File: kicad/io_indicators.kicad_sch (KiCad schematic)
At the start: 68 parts

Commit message: Pick JLCPCB parts for the whole BOM and add BOM/CPL generation
Adds bom/parts.csv (LCSC numbers and MPNs), scripts to apply it to the schematic and
board and to generate the JLCPCB BOM, CPL and a live stock report. Swaps the
BOOTSEL/RESET switch to a basic 5.1 mm part with a matching footprint, and replaces
out-of-stock parts (SS54, WS2812B, 10u caps, SWD header).

Co-Authored-By: Claude Sonnet 5.5 <noreply@anthropic.com>
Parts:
- R100, R101, R72, R73, R74, R75, R76, R77, R78, R79, R80, R81, R82, R83, R84, R85, R86, R87, R88, R89, R90, R91, R92, R93, R94, R95, R96, R97, R98, R99: LCSC (none) -> C25117; MPN (none) -> 0402WGF4700TCE
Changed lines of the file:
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@@
+      (effects (font (size 1.27 1.27)) hide)
+    )
+    (property "LCSC" "C25117" (id 4) (at 40.132 76.2 0)
+      (effects (font (size 1.27 1.27)) hide)
+    )
+    (property "MPN" "0402WGF4700TCE" (id 5) (at 40.132 76.2 0)
       (effects (font (size 1.27 1.27)) hide)
     )
@@
       (effects (font (size 1.27 1.27)) hide)
     )
+    (property "LCSC" "C25117" (id 4) (at 65.532 76.2 0)
+      (effects (font (size 1.27 1.27)) hide)
+    )
+    (property "MPN" "0402WGF4700TCE" (id 5) (at 65.532 76.2 0)
+      (effects (font (size 1.27 1.27)) hide)
+    )
     (pin "1")
     (pin "2")
@@
       (effects (font (size 1.27 1.27)) hide)
     )
+    (property "LCSC" "C25117" (id 4) (at 90.932 76.2 0)
+      (effects (font (size 1.27 1.27)) hide)
+    )
+    (property "MPN" "0402WGF4700TCE" (id 5) (at 90.932 76.2 0)
+      (effects (font (size 1.27 1.27)) hide)
+    )
     (pin "1")
     (pin "2")
@@
       (effects (font (size 1.27 1.27)) hide)
     )
+    (property "LCSC" "C25117" (id 4) (at 116.332 76.2 0)
+      (effects (font (size 1.27 1.27)) hide)
+    )
+    (property "MPN" "0402WGF4700TCE" (id 5) (at 116.332 76.2 0)
+      (effects (font (size 1.27 1.27)) hide)
+    )
     (pin "1")
     (pin "2")
@@
       (effects (font (size 1.27 1.27)) hide)
     )
+    (property "LCSC" "C25117" (id 4) (at 141.732 76.2 0)
+      (effects (font (size 1.27 1.27)) hide)
+    )
+    (property "MPN" "0402WGF4700TCE" (id 5) (at 141.732 76.2 0)
+      (effects (font (size 1.27 1.27)) hide)
+    )
     (pin "1")
     (pin "2")
@@
       (effects (font (size 1.27 1.27)) hide)
     )
+    (property "LCSC" "C25117" (id 4) (at 167.132 76.2 0)
+      (effects (font (size 1.27 1.27)) hide)
+    )
+    (property "MPN" "0402WGF4700TCE" (id 5) (at 167.132 76.2 0)
+      (effects (font (size 1.27 1.27)) hide)
+    )
     (pin "1")
     (pin "2")
@@
       (effects (font (size 1.27 1.27)) hide)
     )
+    (property "LCSC" "C25117" (id 4) (at 192.532 76.2 0)
+      (effects (font (size 1.27 1.27)) hide)
+    )
+    (property "MPN" "0402WGF4700TCE" (id 5) (at 192.532 76.2 0)
+      (effects (font (size 1.27 1.27)) hide)
+    )
     (pin "1")
     (pin "2")
@@
       (effects (font (size 1.27 1.27)) hide)
     )
+    (property "LCSC" "C25117" (id 4) (at 217.932 76.2 0)
+      (effects (font (size 1.27 1.27)) hide)
+    )
+    (property "MPN" "0402WGF4700TCE" (id 5) (at 217.932 76.2 0)
+      (effects (font (size 1.27 1.27)) hide)
+    )
     (pin "1")
     (pin "2")
@@
       (effects (font (size 1.27 1.27)) hide)
     )
+    (property "LCSC" "C25117" (id 4) (at 243.332 76.2 0)
+      (effects (font (size 1.27 1.27)) hide)
+    )
+    (property "MPN" "0402WGF4700TCE" (id 5) (at 243.332 76.2 0)
+      (effects (font (size 1.27 1.27)) hide)
+    )
     (pin "1")
     (pin "2")
@@
       (effects (font (size 1.27 1.27)) hide)
     )
+    (property "LCSC" "C25117" (id 4) (at 268.732 76.2 0)
+      (effects (font (size 1.27 1.27)) hide)
+    )
+    (property "MPN" "0402WGF4700TCE" (id 5) (at 268.732 76.2 0)
+      (effects (font (size 1.27 1.27)) hide)
+    )
     (pin "1")
     (pin "2")
@@
       (effects (font (size 1.27 1.27)) hide)
     )
+    (property "LCSC" "C25117" (id 4) (at 40.132 132.08 0)
+      (effects (font (size 1.27 1.27)) hide)
+    )
+    (property "MPN" "0402WGF4700TCE" (id 5) (at 40.132 132.08 0)
+      (effects (font (size 1.27 1.27)) hide)
+    )
     (pin "1")
     (pin "2")
@@
       (effects (font (size 1.27 1.27)) hide)
     )
+    (property "LCSC" "C25117" (id 4) (at 65.532 132.08 0)
+      (effects (font (size 1.27 1.27)) hide)
+    )
+    (property "MPN" "0402WGF4700TCE" (id 5) (at 65.532 132.08 0)
+      (effects (font (size 1.27 1.27)) hide)
+    )
     (pin "1")
     (pin "2")
@@
       (effects (font (size 1.27 1.27)) hide)
     )
+    (property "LCSC" "C25117" (id 4) (at 90.932 132.08 0)
+      (effects (font (size 1.27 1.27)) hide)
+    )
+    (property "MPN" "0402WGF4700TCE" (id 5) (at 90.932 132.08 0)
+      (effects (font (size 1.27 1.27)) hide)
+    )
     (pin "1")
     (pin "2")
@@
       (effects (font (size 1.27 1.27)) hide)
     )
+    (property "LCSC" "C25117" (id 4) (at 116.332 132.08 0)
+      (effects (font (size 1.27 1.27)) hide)
+    )
+    (property "MPN" "0402WGF4700TCE" (id 5) (at 116.332 132.08 0)
+      (effects (font (size 1.27 1.27)) hide)
+    )
     (pin "1")
     (pin "2")
@@
       (effects (font (size 1.27 1.27)) hide)
     )
+    (property "LCSC" "C25117" (id 4) (at 141.732 132.08 0)
+      (effects (font (size 1.27 1.27)) hide)
+    )
+    (property "MPN" "0402WGF4700TCE" (id 5) (at 141.732 132.08 0)
+      (effects (font (size 1.27 1.27)) hide)
+    )
     (pin "1")
     (pin "2")
@@
       (effects (font (size 1.27 1.27)) hide)
     )
+    (property "LCSC" "C25117" (id 4) (at 167.132 132.08 0)
+      (effects (font (size 1.27 1.27)) hide)
+    )
+    (property "MPN" "0402WGF4700TCE" (id 5) (at 167.132 132.08 0)
+      (effects (font (size 1.27 1.27)) hide)
+    )
     (pin "1")
     (pin "2")
@@
       (effects (font (size 1.27 1.27)) hide)
     )
+    (property "LCSC" "C25117" (id 4) (at 192.532 132.08 0)
+      (effects (font (size 1.27 1.27)) hide)
+    )
+    (property "MPN" "0402WGF4700TCE" (id 5) (at 192.532 132.08 0)
+      (effects (font (size 1.27 1.27)) hide)
+    )
     (pin "1")
     (pin "2")
@@
       (effects (font (size 1.27 1.27)) hide)
     )
+    (property "LCSC" "C25117" (id 4) (at 217.932 132.08 0)
+      (effects (font (size 1.27 1.27)) hide)
+    )
+    (property "MPN" "0402WGF4700TCE" (id 5) (at 217.932 132.08 0)
+      (effects (font (size 1.27 1.27)) hide)
+    )
     (pin "1")
     (pin "2")
@@
       (effects (font (size 1.27 1.27)) hide)
     )
+    (property "LCSC" "C25117" (id 4) (at 243.332 132.08 0)
+      (effects (font (size 1.27 1.27)) hide)
+    )
+    (property "MPN" "0402WGF4700TCE" (id 5) (at 243.332 132.08 0)
+      (effects (font (size 1.27 1.27)) hide)
+    )
     (pin "1")
     (pin "2")
@@
       (effects (font (size 1.27 1.27)) hide)
     )
+    (property "LCSC" "C25117" (id 4) (at 268.732 132.08 0)
+      (effects (font (size 1.27 1.27)) hide)
+    )
+    (property "MPN" "0402WGF4700TCE" (id 5) (at 268.732 132.08 0)
+      (effects (font (size 1.27 1.27)) hide)
+    )
     (pin "1")
     (pin "2")
@@
       (effects (font (size 1.27 1.27)) hide)
     )
+    (property "LCSC" "C25117" (id 4) (at 40.132 187.96 0)
+      (effects (font (size 1.27 1.27)) hide)
+    )
+    (property "MPN" "0402WGF4700TCE" (id 5) (at 40.132 187.96 0)
+      (effects (font (size 1.27 1.27)) hide)
+    )
     (pin "1")
     (pin "2")
@@
       (effects (font (size 1.27 1.27)) hide)
     )
+    (property "LCSC" "C25117" (id 4) (at 65.532 187.96 0)
+      (effects (font (size 1.27 1.27)) hide)
+    )
+    (property "MPN" "0402WGF4700TCE" (id 5) (at 65.532 187.96 0)
+      (effects (font (size 1.27 1.27)) hide)
+    )
     (pin "1")
     (pin "2")
@@
       (effects (font (size 1.27 1.27)) hide)
     )
+    (property "LCSC" "C25117" (id 4) (at 40.132 256.54 0)
+      (effects (font (size 1.27 1.27)) hide)
+    )
+    (property "MPN" "0402WGF4700TCE" (id 5) (at 40.132 256.54 0)
+      (effects (font (size 1.27 1.27)) hide)
+    )
     (pin "1")
     (pin "2")
@@
       (effects (font (size 1.27 1.27)) hide)
     )
+    (property "LCSC" "C25117" (id 4) (at 65.532 256.54 0)
+      (effects (font (size 1.27 1.27)) hide)
+    )
+    (property "MPN" "0402WGF4700TCE" (id 5) (at 65.532 256.54 0)
+      (effects (font (size 1.27 1.27)) hide)
+    )
     (pin "1")
     (pin "2")
@@
       (effects (font (size 1.27 1.27)) hide)
     )
+    (property "LCSC" "C25117" (id 4) (at 90.932 256.54 0)
+      (effects (font (size 1.27 1.27)) hide)
+    )
+    (property "MPN" "0402WGF4700TCE" (id 5) (at 90.932 256.54 0)
+      (effects (font (size 1.27 1.27)) hide)
+    )
     (pin "1")
     (pin "2")
@@
       (effects (font (size 1.27 1.27)) hide)
     )
+    (property "LCSC" "C25117" (id 4) (at 116.332 256.54 0)
+      (effects (font (size 1.27 1.27)) hide)
+    )
+    (property "MPN" "0402WGF4700TCE" (id 5) (at 116.332 256.54 0)
+      (effects (font (size 1.27 1.27)) hide)
+    )
     (pin "1")
     (pin "2")
@@
       (effects (font (size 1.27 1.27)) hide)
     )
+    (property "LCSC" "C25117" (id 4) (at 141.732 256.54 0)
+      (effects (font (size 1.27 1.27)) hide)
+    )
+    (property "MPN" "0402WGF4700TCE" (id 5) (at 141.732 256.54 0)
+      (effects (font (size 1.27 1.27)) hide)
+    )
     (pin "1")
     (pin "2")
@@
       (effects (font (size 1.27 1.27)) hide)
     )
+    (property "LCSC" "C25117" (id 4) (at 167.132 256.54 0)
+      (effects (font (size 1.27 1.27)) hide)
+    )
+    (property "MPN" "0402WGF4700TCE" (id 5) (at 167.132 256.54 0)
+      (effects (font (size 1.27 1.27)) hide)
+    )
     (pin "1")
     (pin "2")
@@
       (effects (font (size 1.27 1.27)) hide)
     )
+    (property "LCSC" "C25117" (id 4) (at 192.532 256.54 0)
+      (effects (font (size 1.27 1.27)) hide)
+    )
+    (property "MPN" "0402WGF4700TCE" (id 5) (at 192.532 256.54 0)
+      (effects (font (size 1.27 1.27)) hide)
+    )
     (pin "1")
     (pin "2")
@@
       (effects (font (size 1.27 1.27)) hide)
     )
+    (property "LCSC" "C25117" (id 4) (at 217.932 256.54 0)
+      (effects (font (size 1.27 1.27)) hide)
+    )
+    (property "MPN" "0402WGF4700TCE" (id 5) (at 217.932 256.54 0)
+      (effects (font (size 1.27 1.27)) hide)
+    )

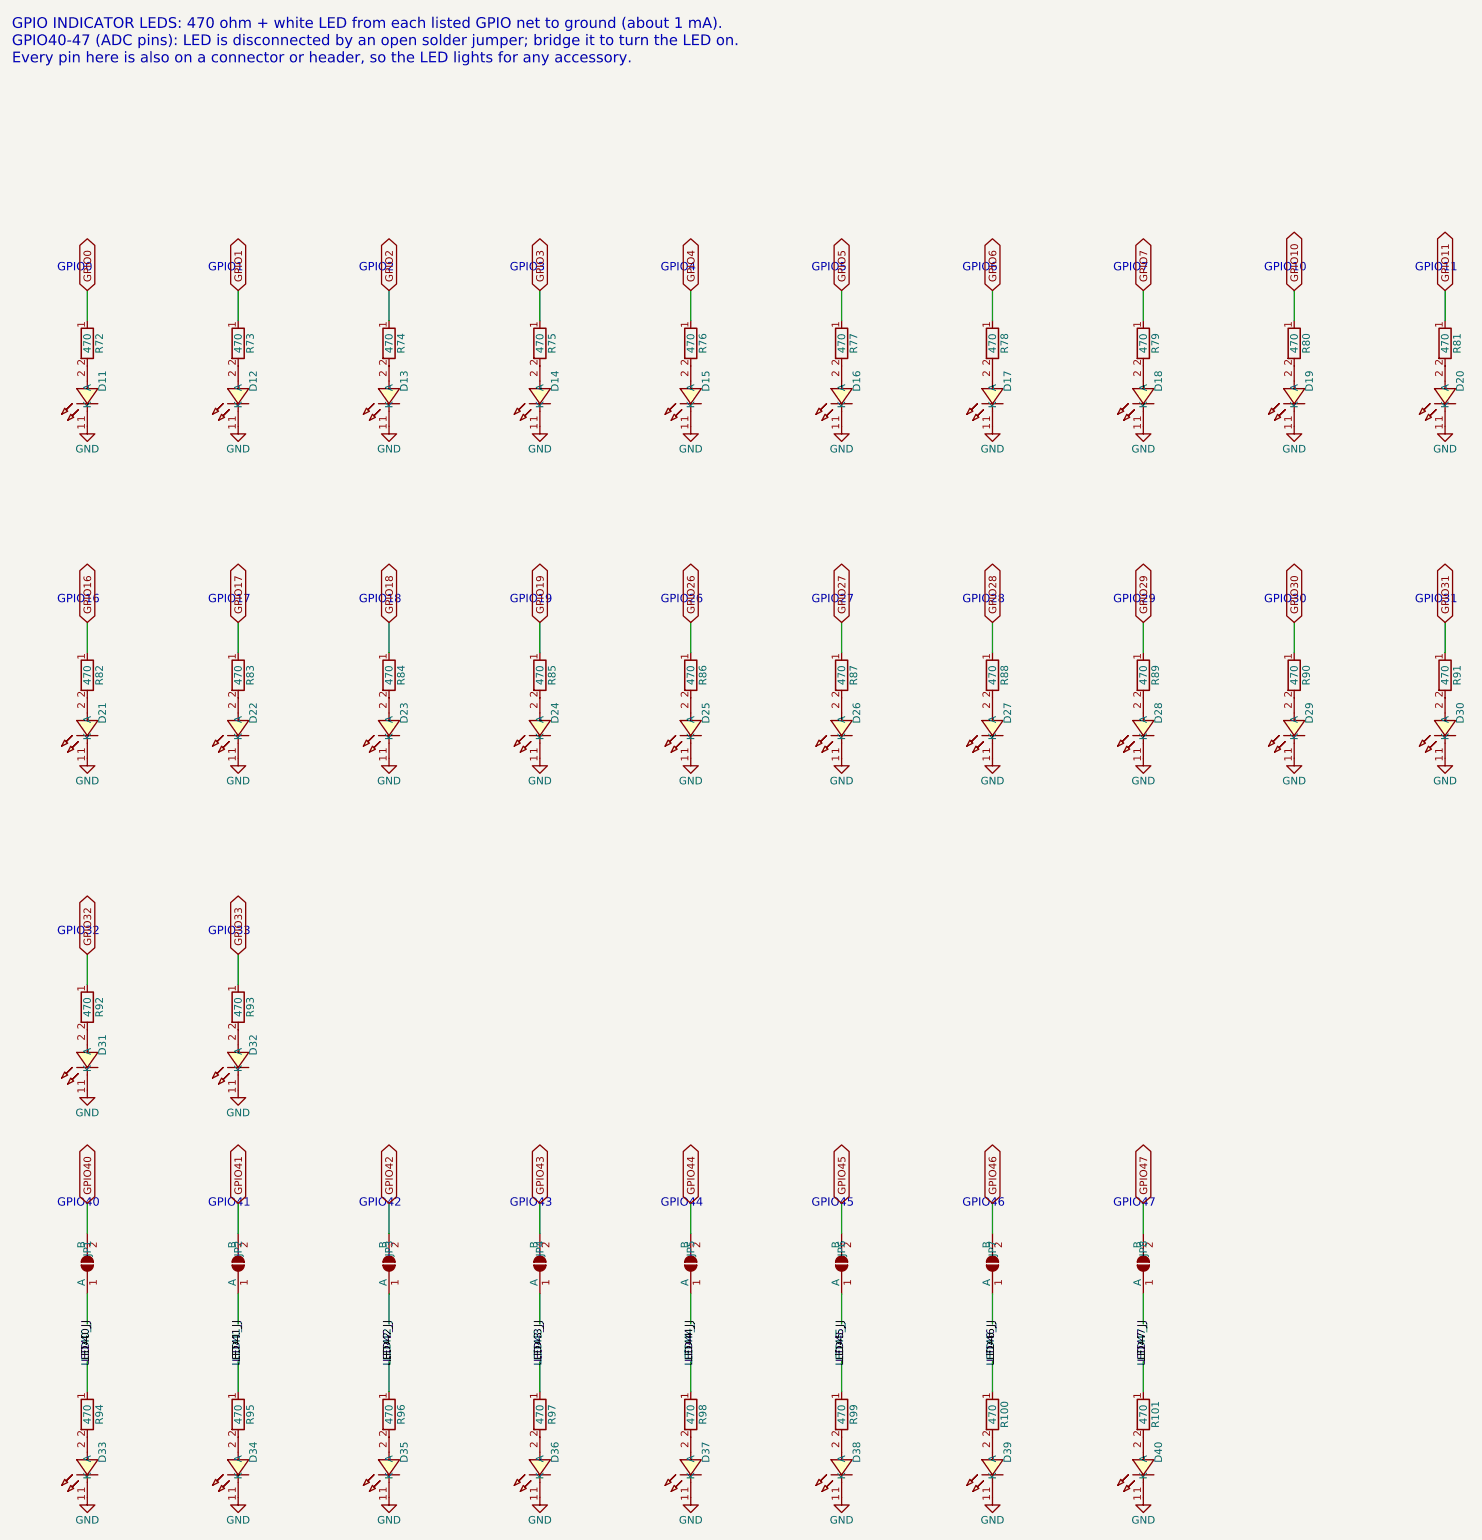
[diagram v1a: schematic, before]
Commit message: Rework board layout, swap SWD header to through-hole, add Qwiic port
- SWD (J10) is now a 1x3 2.54 mm through-hole pin header footprint
  (SWCLK, GND, SWDIO) instead of the JST SH connector; removed from the
  JLCPCB BOM.
- Add J20 Qwiic connector (XY-SM04B-SRSS-TB) on the I2C bus: GND, +3V3,
  GPIO20 (SDA), GPIO21 (SCL), mounting tabs to GND.
- Placement/routing progress and the helper scripts used for it.

DRC still reports open items (unrouted RUN/GPIO24/GPIO29/QSPI_SD0 nets,
R108/GPIO23 and NT1/GPIO20 shorts, J12 edge clearance, silkscreen
overlaps); to be fixed in follow-up commits.

Co-Authored-By: Claude Sonnet 5.5 <noreply@anthropic.com>
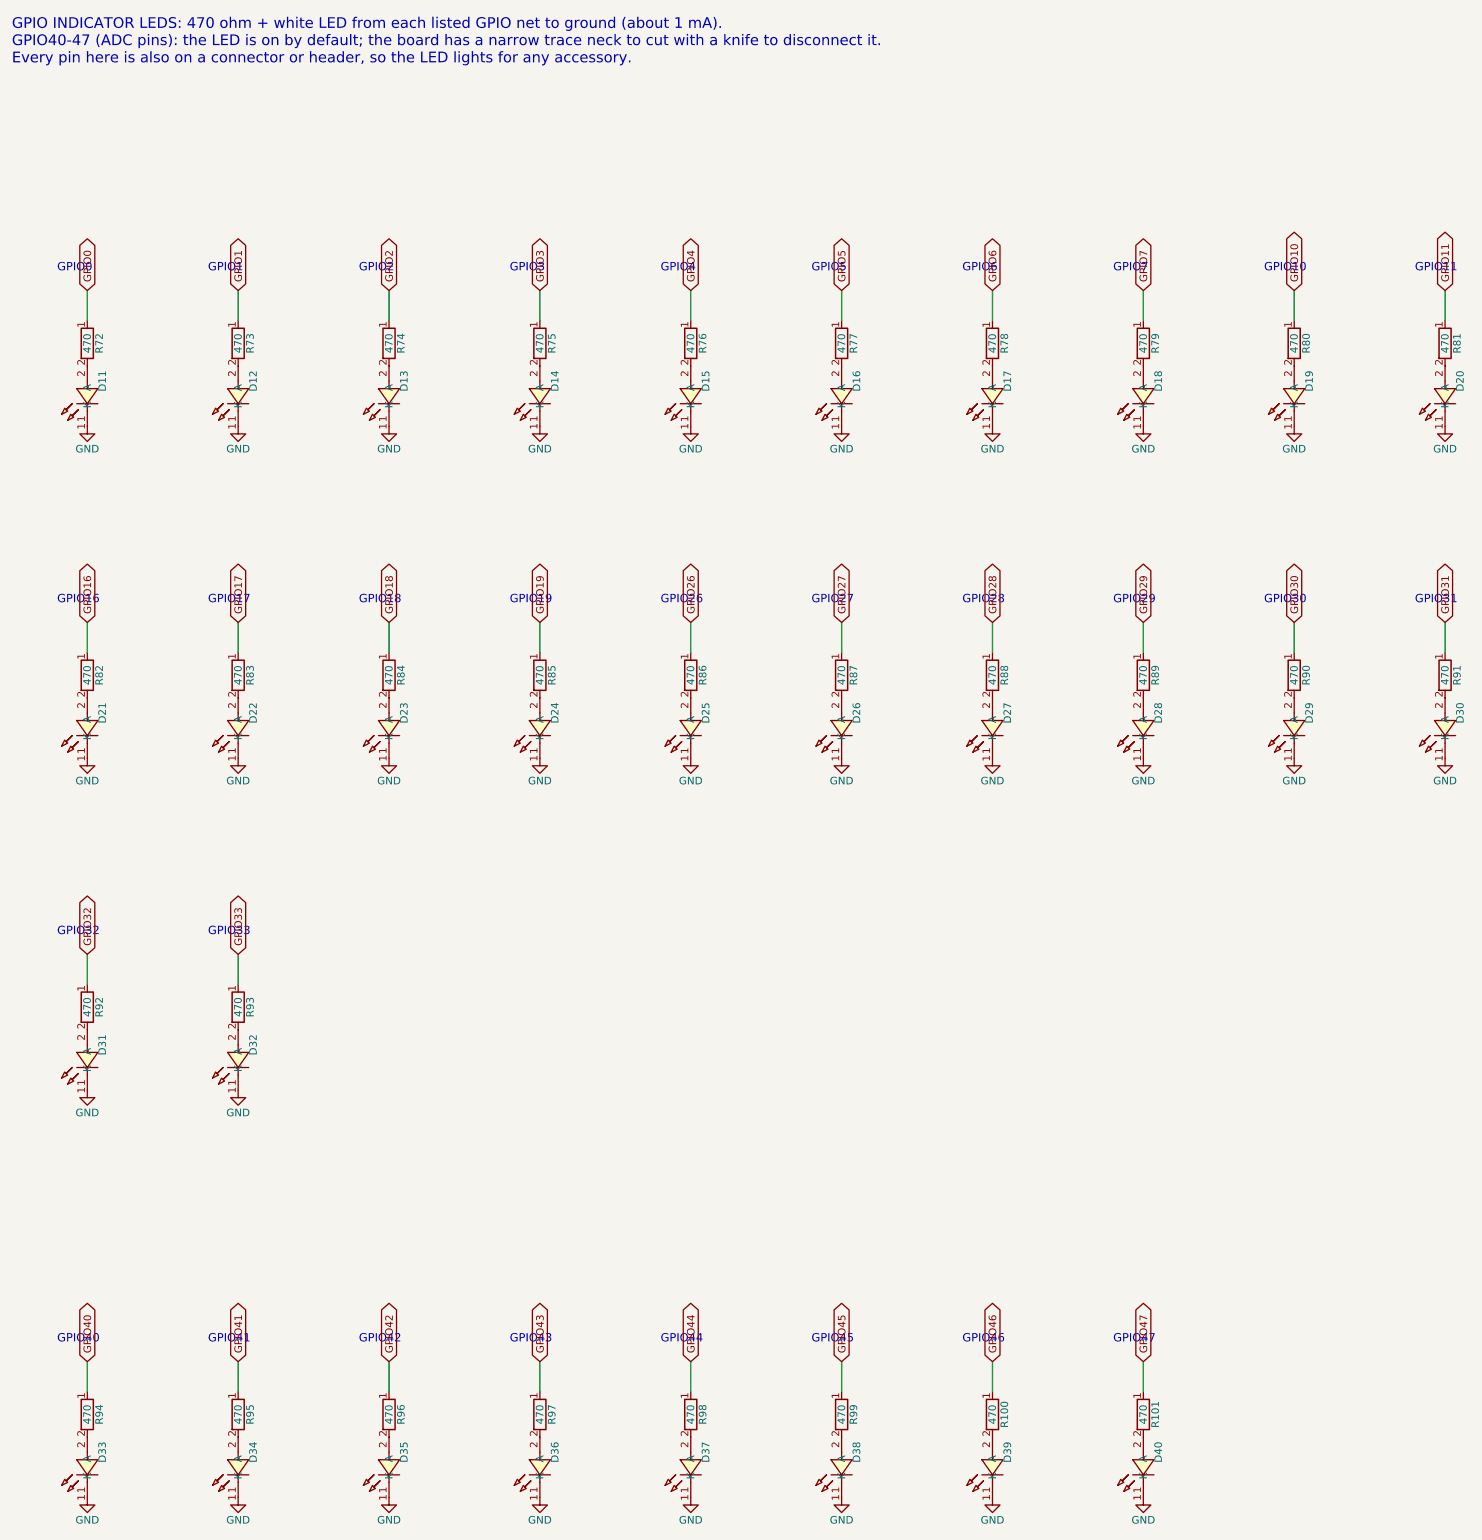
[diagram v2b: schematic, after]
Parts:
- removed JP1, JP2, JP3, JP4, JP5, JP6, JP7, JP8: LED enable, Jumper:SolderJumper-2_P1.3mm_Open_RoundedPad1.0x1.5mm, symbol Jumper:SolderJumper_2_Open
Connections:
- net LED40_J is gone; now on net GPIO40: R94.1
- net LED41_J is gone; now on net GPIO41: R95.1
- net LED42_J is gone; now on net GPIO42: R96.1
- net LED43_J is gone; now on net GPIO43: R97.1
- net LED44_J is gone; now on net GPIO44: R98.1
- net LED45_J is gone; now on net GPIO45: R99.1
- net LED46_J is gone; now on net GPIO46: R100.1
- net LED47_J is gone; now on net GPIO47: R101.1
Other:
- note added: "GPIO INDICATOR LEDS: 470 ohm + white LED from each listed GPIO net to ground (about 1 mA). GPIO40-47 (ADC pins): the LED is on by default; the board has a narrow trace neck to cut with a knife to disconnect it. Every pin here is also on a connector or header, so the LED lights for any accessory."
- note removed: "GPIO INDICATOR LEDS: 470 ohm + white LED from each listed GPIO net to ground (about 1 mA). GPIO40-47 (ADC pins): LED is disconnected by an open solder jumper; bridge it to turn the LED on. Every pin here is also on a connector or header, so the LED lights for any accessory."
